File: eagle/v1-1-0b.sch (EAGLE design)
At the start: 176 parts, among them J1 CR22A-44D-2.54DSA(70), J3 26-60-4040, J4 AUDIO_JACK_3.5MM_PTH, J5 DIN5, SW1 3PDT-AQ-SWITCH, SW2 9077-1, U10 7805, U11 74LS10N, U13 74LS04N, U14 4528N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

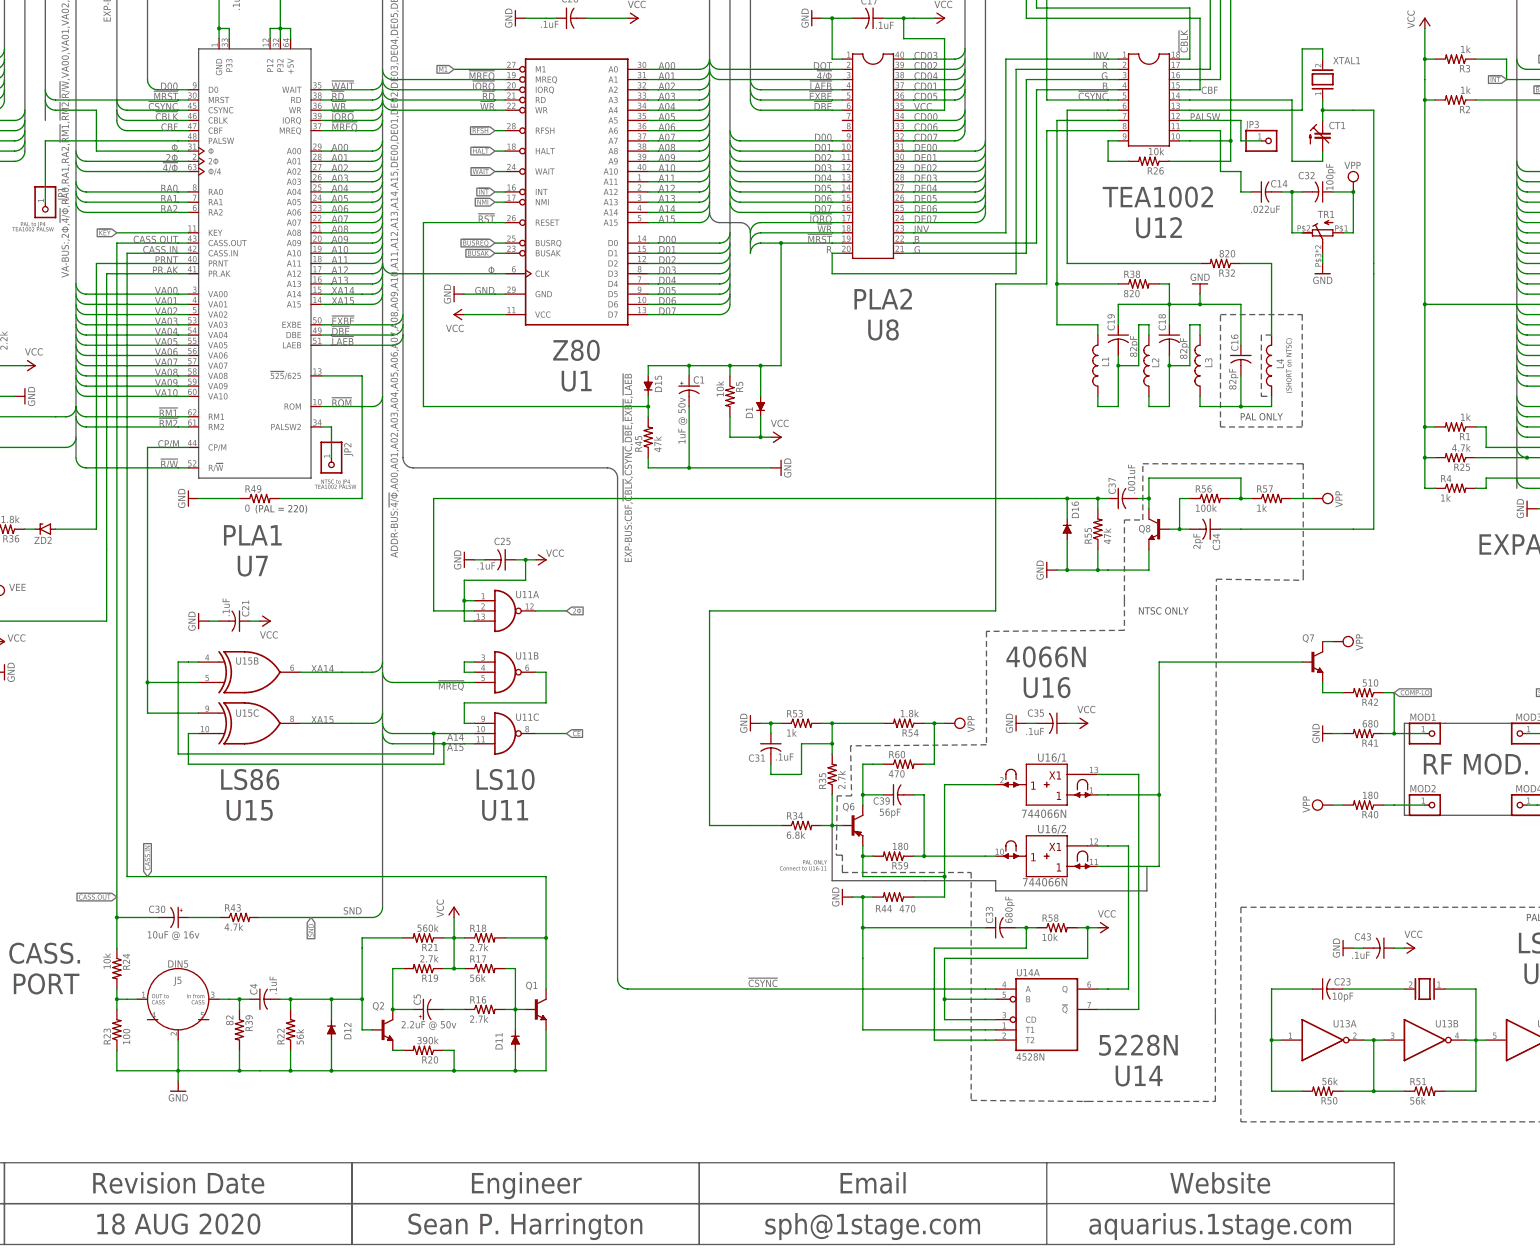
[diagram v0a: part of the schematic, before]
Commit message: Edits for component values
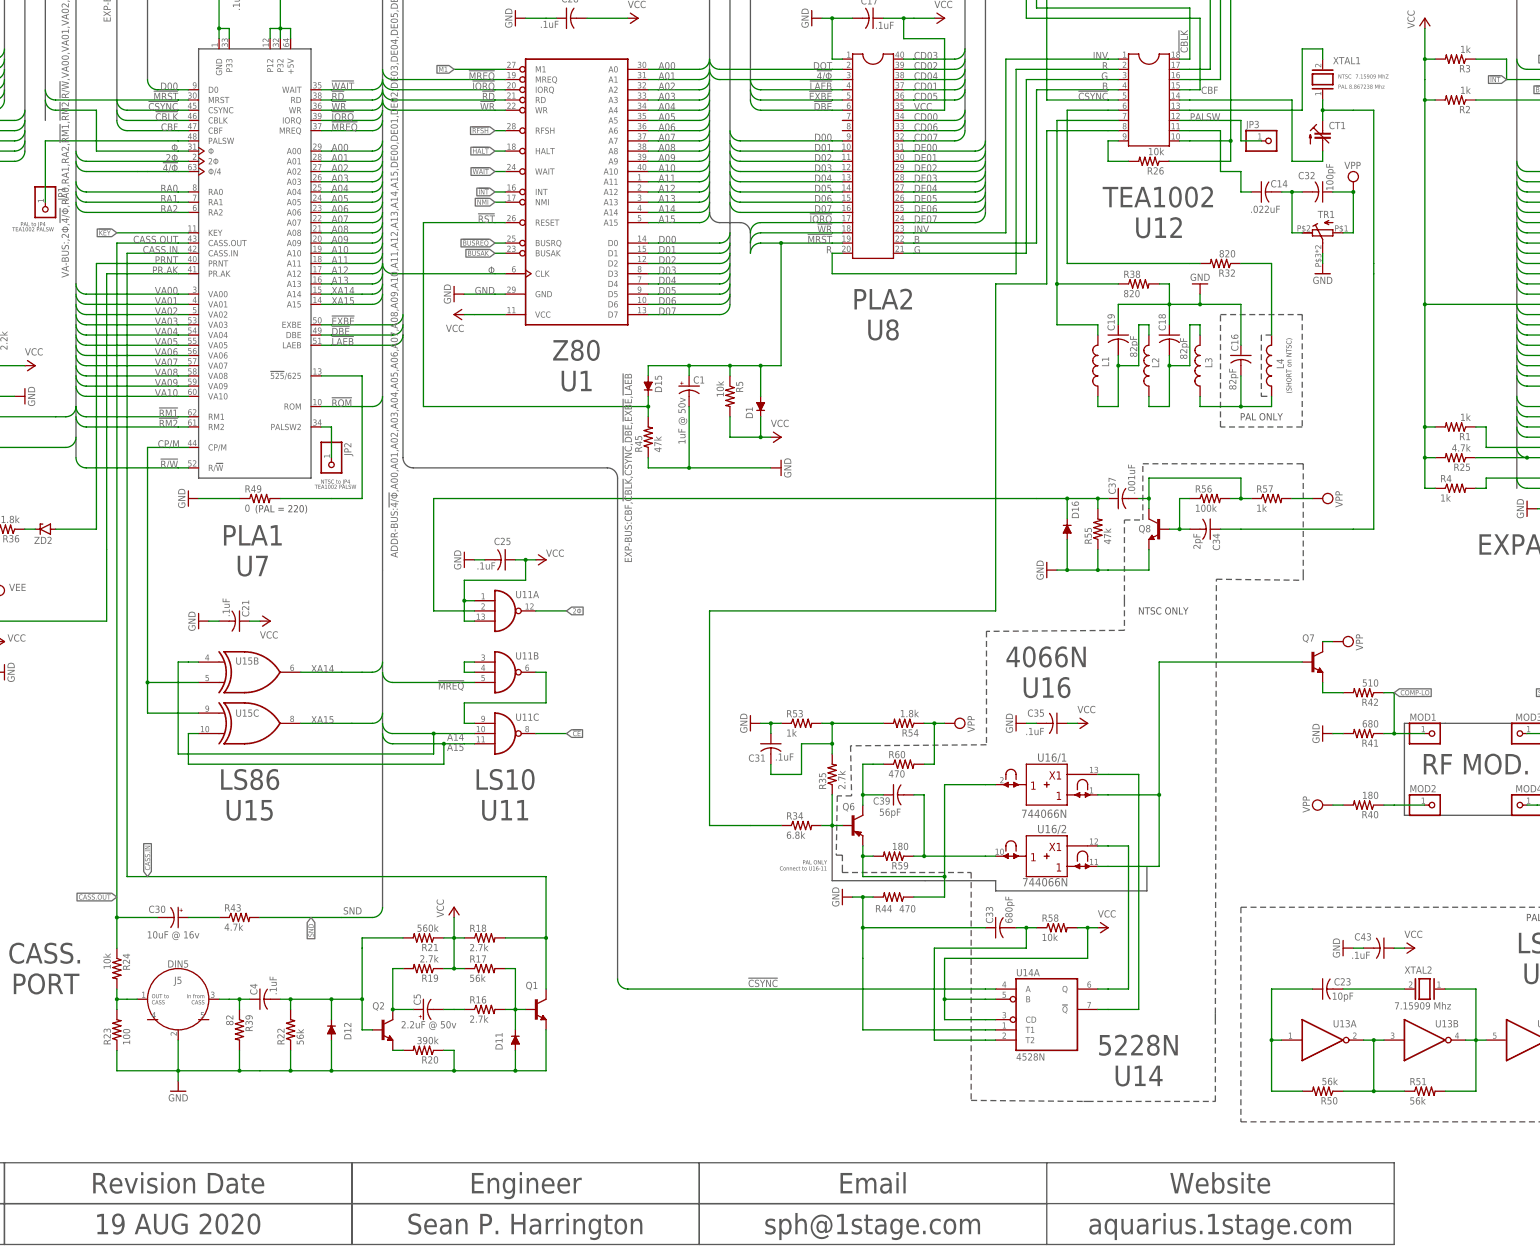
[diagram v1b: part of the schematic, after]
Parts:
- XTAL1: value (none) -> 7.15909 MhZ
- XTAL2: value (none) -> 7.15909 Mhz
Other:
- note added: "19 AUG 2020"
- note added: "NTSC"
- note added: "PAL 8.867238 Mhz"
- note removed: "18 AUG 2020"
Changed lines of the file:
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@@
 <part name="C31" library="aq-rcl" deviceset="C-US" device="050-024X044" package3d_urn="urn:adsk.eagle:package:23643/1" value=".1uF"/>
 <part name="C29" library="aq-rcl" deviceset="C-US" device="050-024X044" package3d_urn="urn:adsk.eagle:package:23643/1" value="150pF"/>
-<part name="XTAL1" library="special" library_urn="urn:adsk.eagle:library:367" deviceset="XTAL" device="" package3d_urn="urn:adsk.eagle:package:26649/1"/>
+<part name="XTAL1" library="special" library_urn="urn:adsk.eagle:library:367" deviceset="XTAL" device="" package3d_urn="urn:adsk.eagle:package:26649/1" value="7.15909 MhZ"/>
 <part name="CT1" library="aq-rcl" deviceset="C-TRIMM" device="808" package3d_urn="urn:adsk.eagle:package:23766/1"/>
 <part name="SW1" library="aquarius" deviceset="3PDT-AQ-SWITCH" device=""/>
@@
 <part name="R50" library="aq-rcl" deviceset="R-US_" device="0207/10" package3d_urn="urn:adsk.eagle:package:23491/2" value="56k"/>
 <part name="R51" library="aq-rcl" deviceset="R-US_" device="0207/10" package3d_urn="urn:adsk.eagle:package:23491/2" value="56k"/>
-<part name="XTAL2" library="special" library_urn="urn:adsk.eagle:library:367" deviceset="XTAL" device="" package3d_urn="urn:adsk.eagle:package:26649/1"/>
+<part name="XTAL2" library="special" library_urn="urn:adsk.eagle:library:367" deviceset="XTAL" device="" package3d_urn="urn:adsk.eagle:package:26649/1" value="7.15909 Mhz"/>
 <part name="R52" library="aq-rcl" deviceset="R-US_" device="0207/10" package3d_urn="urn:adsk.eagle:package:23491/2" value="56k"/>
 <part name="U13" library="74xx-us" library_urn="urn:adsk.eagle:library:88" deviceset="74*04" device="N" package3d_urn="urn:adsk.eagle:package:16407/2" technology="LS"/>
@@
 <wire x1="261.62" y1="15.24" x2="261.62" y2="5.08" width="0.1524" layer="97"/>
 <wire x1="261.62" y1="5.08" x2="347.98" y2="5.08" width="0.1524" layer="97"/>
-<text x="304.8" y="7.62" size="5.08" layer="97" align="bottom-center">18 AUG 2020</text>
+<text x="304.8" y="7.62" size="5.08" layer="97" align="bottom-center">19 AUG 2020</text>
 <wire x1="347.98" y1="15.24" x2="347.98" y2="25.4" width="0.1524" layer="97"/>
 <wire x1="347.98" y1="25.4" x2="261.62" y2="25.4" width="0.1524" layer="97"/>
@@
 <wire x1="469.9" y1="101.854" x2="469.9" y2="99.06" width="0.1524" layer="97" style="shortdash"/>
 <wire x1="562.864" y1="170.434" x2="584.2" y2="170.18" width="0.1524" layer="97" style="shortdash"/>
+<text x="593.09" y="292.354" size="1.016" layer="96">PAL 8.867238 Mhz</text>
+<text x="593.09" y="294.894" size="1.016" layer="96">NTSC</text>
 </plain>
 <instances>
@@
 <instance part="XTAL1" gate="G$1" x="589.28" y="294.64" smashed="yes" rot="R90">
 <attribute name="NAME" x="591.82" y="298.45" size="1.778" layer="95"/>
-<attribute name="VALUE" x="594.36" y="289.56" size="1.778" layer="96" rot="R90"/>
+<attribute name="VALUE" x="597.408" y="294.894" size="1.016" layer="96"/>
 </instance>
 <instance part="CT1" gate="G$1" x="589.28" y="281.94" smashed="yes">
@@
 </instance>
 <instance part="XTAL2" gate="G$1" x="614.68" y="68.58" smashed="yes" rot="R180">
-<attribute name="VALUE" x="619.76" y="73.66" size="1.778" layer="96" rot="R180"/>
+<attribute name="NAME" x="609.6" y="72.39" size="1.778" layer="95"/>
+<attribute name="VALUE" x="607.06" y="63.5" size="1.778" layer="96"/>
 </instance>
 <instance part="R52" gate="G$1" x="657.86" y="55.88" smashed="yes" rot="R180">
